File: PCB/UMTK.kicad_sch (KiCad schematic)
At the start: 10 parts

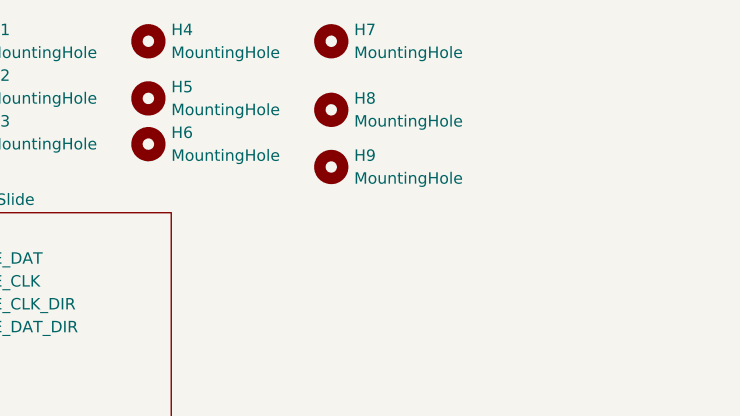
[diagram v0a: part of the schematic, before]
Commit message: Update PCB to seperate ground symbols apporiately. Modify board to sepearte ground path for motor current and all other devices. Add filtering for slide power, hopefully reduce bownout or other issue.
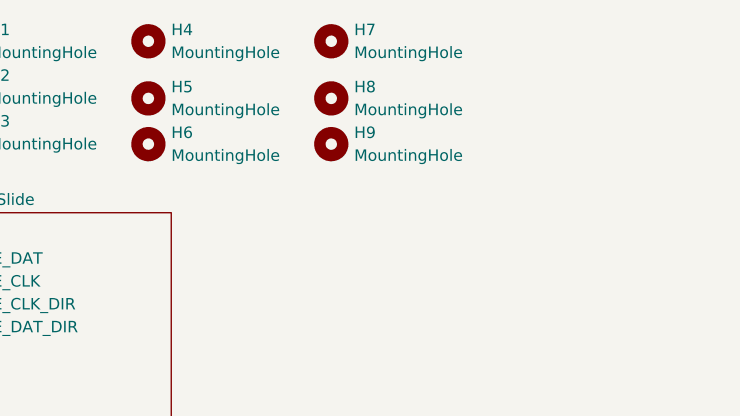
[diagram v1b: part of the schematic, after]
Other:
- moved on the sheet: H8, H9
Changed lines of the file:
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@@
 	(symbol
 		(lib_id "Mechanical:MountingHole")
-		(at 208.28 26.67 0)
+		(at 208.28 25.4 0)
 		(unit 1)
 		(exclude_from_sim yes)
@@
 		(fields_autoplaced yes)
 		(property "Reference" "H8"
-			(at 210.82 25.3999 0)
+			(at 210.82 24.1299 0)
 			(effects
 				(font
@@
 		)
 		(property "Value" "MountingHole"
-			(at 210.82 27.9399 0)
+			(at 210.82 26.6699 0)
 			(effects
 				(font
@@
 		)
 		(property "Footprint" "MountingHole:MountingHole_4mm"
-			(at 208.28 26.67 0)
+			(at 208.28 25.4 0)
 			(effects
 				(font
@@
 		)
 		(property "Datasheet" "~"
-			(at 208.28 26.67 0)
+			(at 208.28 25.4 0)
 			(effects
 				(font
@@
 		)
 		(property "Description" "Mounting Hole without connection"
-			(at 208.28 26.67 0)
+			(at 208.28 25.4 0)
 			(effects
 				(font
@@
 	(symbol
 		(lib_id "Mechanical:MountingHole")
-		(at 208.28 33.02 0)
+		(at 208.28 30.48 0)
 		(unit 1)
 		(exclude_from_sim yes)
@@
 		(fields_autoplaced yes)
 		(property "Reference" "H9"
+			(at 210.82 29.2099 0)
+			(effects
+				(font
+					(size 1.27 1.27)
+				)
+				(justify left)
+			)
+		)
+		(property "Value" "MountingHole"
 			(at 210.82 31.7499 0)
 			(effects
@@
 			)
 		)
-		(property "Value" "MountingHole"
-			(at 210.82 34.2899 0)
-			(effects
-				(font
-					(size 1.27 1.27)
-				)
-				(justify left)
-			)
-		)
 		(property "Footprint" "MountingHole:MountingHole_4mm"
-			(at 208.28 33.02 0)
+			(at 208.28 30.48 0)
 			(effects
 				(font
@@
 		)
 		(property "Datasheet" "~"
-			(at 208.28 33.02 0)
+			(at 208.28 30.48 0)
 			(effects
 				(font
@@
 		)
 		(property "Description" "Mounting Hole without connection"
-			(at 208.28 33.02 0)
-			(effects
-				(font
+			(at 208.28 30.48 0)
+			(effects
+				(font

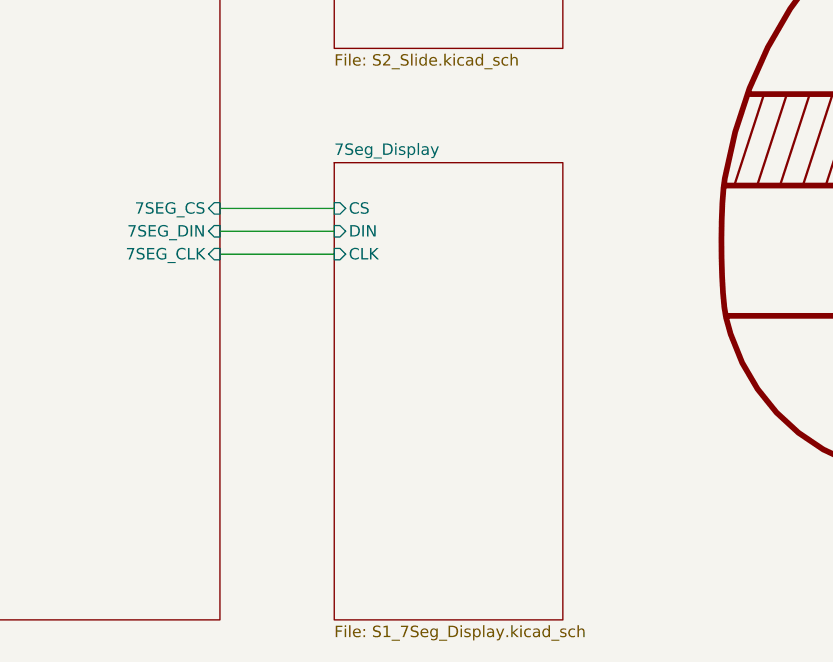
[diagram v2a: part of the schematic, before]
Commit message: Schematic bit done for adding arduino, improved motor maybe a bit by adding caps, improved slide a bit by adding protection and more caps
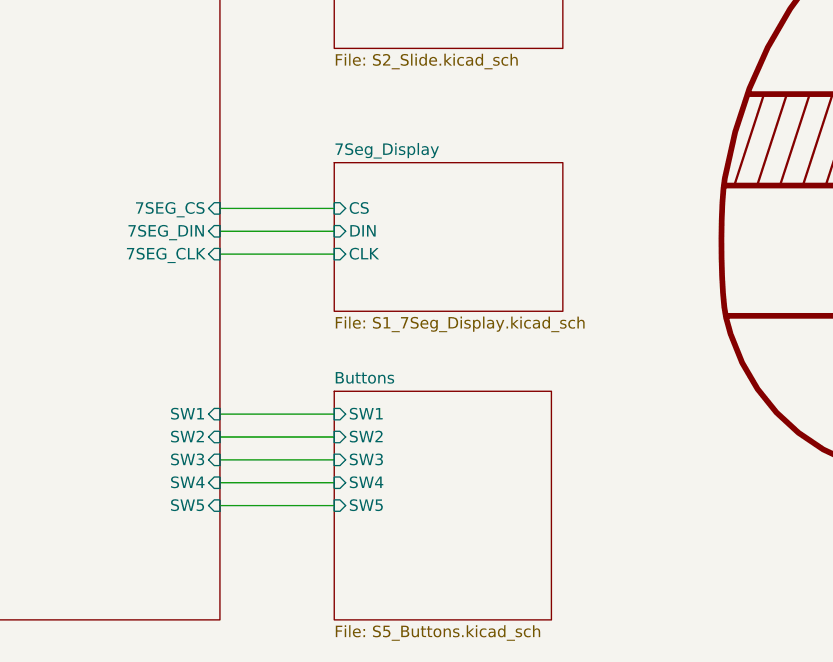
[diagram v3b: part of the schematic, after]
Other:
- added sheet Buttons (S5_Buttons.kicad_sch)
- sheet Arduino ports: added SW1, SW2, SW3, SW4, SW5; removed none
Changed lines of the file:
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@@
+	(wire
+		(pts
+			(xy 152.4 116.84) (xy 165.1 116.84)
+		)
+		(stroke
+			(width 0)
+			(type default)
+		)
+	)
 	(wire
 		(pts
@@
 	(wire
 		(pts
+			(xy 152.4 121.92) (xy 165.1 121.92)
+		)
+		(stroke
+			(width 0)
+			(type default)
+		)
+	)
+	(wire
+		(pts
+			(xy 152.4 124.46) (xy 165.1 124.46)
+		)
+		(stroke
+			(width 0)
+			(type default)
+		)
+	)
+	(wire
+		(pts
+			(xy 152.4 119.38) (xy 165.1 119.38)
+		)
+		(stroke
+			(width 0)
+			(type default)
+		)
+	)
+	(wire
+		(pts
 			(xy 88.9 96.52) (xy 101.6 96.52)
 		)
@@
 		(pts
 			(xy 152.4 96.52) (xy 165.1 96.52)
+		)
+		(stroke
+			(width 0)
+			(type default)
+		)
+	)
+	(wire
+		(pts
+			(xy 152.4 127) (xy 165.1 127)
 		)
 		(stroke
@@
 			)
 		)
+		(pin "SW1" input
+			(at 152.4 116.84 0)
+			(effects
+				(font
+					(size 1.27 1.27)
+				)
+				(justify right)
+			)
+		)
+		(pin "SW2" input
+			(at 152.4 119.38 0)
+			(effects
+				(font
+					(size 1.27 1.27)
+				)
+				(justify right)
+			)
+		)
+		(pin "SW3" input
+			(at 152.4 121.92 0)
+			(effects
+				(font
+					(size 1.27 1.27)
+				)
+				(justify right)
+			)
+		)
+		(pin "SW4" input
+			(at 152.4 124.46 0)
+			(effects
+				(font
+					(size 1.27 1.27)
+				)
+				(justify right)
+			)
+		)
+		(pin "SW5" input
+			(at 152.4 127 0)
+			(effects
+				(font
+					(size 1.27 1.27)
+				)
+				(justify right)
+			)
+		)
 		(instances
 			(project "UMTK"
@@
 	(sheet
 		(at 165.1 88.9)
-		(size 25.4 50.8)
+		(size 25.4 16.51)
 		(exclude_from_sim no)
 		(in_bom yes)
@@
 		)
 		(property "Sheetfile" "S1_7Seg_Display.kicad_sch"
-			(at 165.1 140.2846 0)
+			(at 165.1 105.9946 0)
 			(effects
 				(font
@@
 				)
 			)
+		)
+	)
+	(sheet
+		(at 165.1 114.3)
+		(size 24.13 25.4)
+		(exclude_from_sim no)
+		(in_bom yes)
+		(on_board yes)
+		(dnp no)
+		(fields_autoplaced yes)
+		(stroke
+			(width 0.1524)
+			(type solid)
+		)
+		(fill
+			(color 0 0 0 0.0000)
+		)
+		(property "Sheetname" "Buttons"
+			(at 165.1 113.5884 0)
+			(effects
+				(font
+					(size 1.27 1.27)
+				)
+				(justify left bottom)
+			)
+		)
+		(property "Sheetfile" "S5_Buttons.kicad_sch"
+			(at 165.1 140.2846 0)
+			(effects
+				(font
+					(size 1.27 1.27)
+				)
+				(justify left top)
+			)
+		)
+		(pin "SW1" input
+			(at 165.1 116.84 180)
+			(effects
+				(font
+					(size 1.27 1.27)
+				)
+				(justify left)
+			)
+		)
+		(pin "SW2" input
+			(at 165.1 119.38 180)
+			(effects
+				(font
+					(size 1.27 1.27)
+				)
+				(justify left)
+			)
+		)
+		(pin "SW3" input
+			(at 165.1 121.92 180)
+			(effects
+				(font
+					(size 1.27 1.27)
+				)
+				(justify left)
+			)
+		)
+		(pin "SW4" input
+			(at 165.1 124.46 180)
+			(effects
+				(font
+					(size 1.27 1.27)
+				)
+				(justify left)
+			)
+		)
+		(pin "SW5" input
+			(at 165.1 127 180)
+			(effects
+				(font
+					(size 1.27 1.27)
+				)
+				(justify left)
+			)
+		)
+		(instances
+			(project "UMTK"
+				(path "/2bf3ea67-58b8-47b3-a768-ea6950b40edf"
+					(page "8")
+				)
+			)
